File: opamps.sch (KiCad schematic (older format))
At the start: 25 parts, among them U501 TSV324IDT, U502 TSV324IDT, U503 TSV324IDT

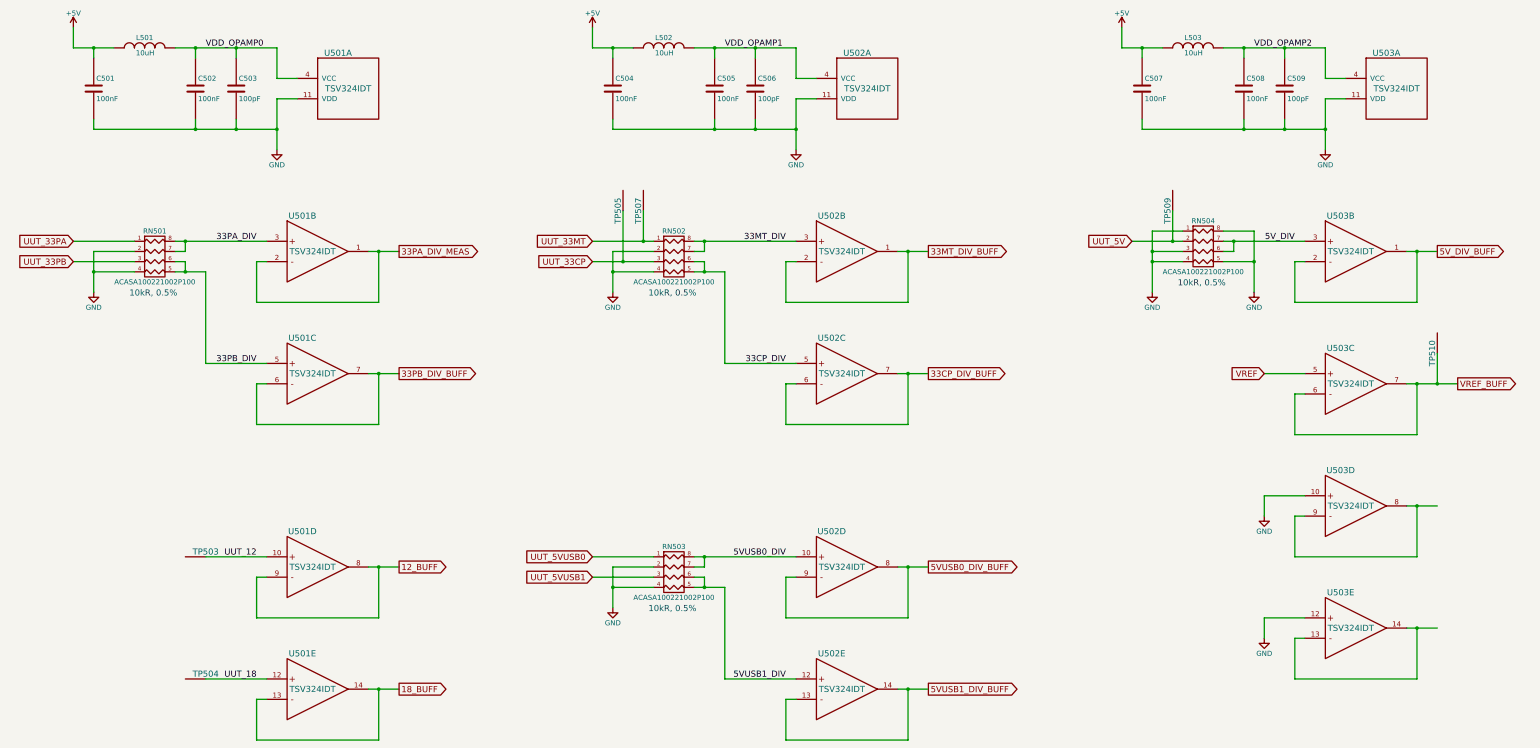
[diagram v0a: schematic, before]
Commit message: significant progress on placement, sch changes for adc routing
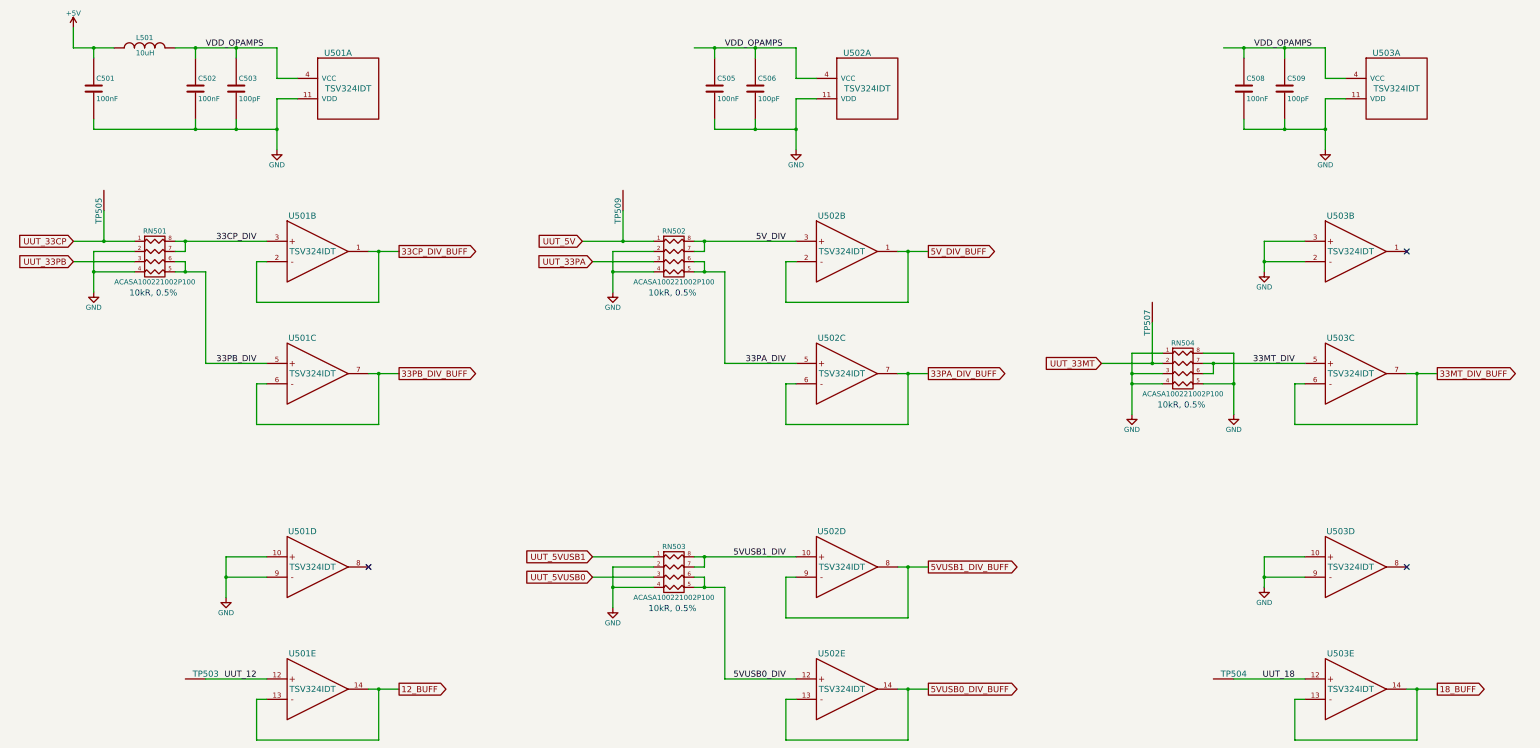
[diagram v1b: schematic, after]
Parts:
- removed C504, C507: 100nF, tm-kicad-lib:SMD-0402-C, symbol TM_C
- removed L502, L503: 10uH, tm-kicad-lib:SMD-0603-R, symbol TM_L
- removed TP510: TP, tm-kicad-lib:Testpoint, symbol TP
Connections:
- net 33PA_DIV_MEAS is gone; now on net 33CP_DIV_BUFF: U501.1, U501.2
- net VDD_OPAMP1 is gone; now on net VDD_OPAMPS: C505.1, C506.1, U502.4 (VCC)
- net VDD_OPAMP2 is gone; now on net VDD_OPAMPS: C508.1, C509.1, U503.4 (VCC)
- net VREF is gone; now on net 33MT_DIV: U503.5
- net VREF_BUFF is gone; now on net 33MT_DIV_BUFF: U503.6, U503.7
- net 12_BUFF: now also U501.13, U501.14; no longer U501.8, U501.9
- net 18_BUFF: now also U503.13, U503.14; no longer U501.13, U501.14
- net 33CP_DIV: now also RN501.7 (R2), RN501.8 (R1), U501.3; no longer RN502.5 (R4), RN502.6 (R3), U502.5
- net 33CP_DIV_BUFF: no longer U502.6, U502.7
- net 33MT_DIV: now also RN504.6 (R3), RN504.7 (R2); no longer RN502.7 (R2), RN502.8 (R1), U502.3
- net 33MT_DIV_BUFF: no longer U502.1, U502.2
- net 33PA_DIV: now also RN502.5 (R4), RN502.6 (R3), U502.5; no longer RN501.7 (R2), RN501.8 (R1), U501.3
- net 5VUSB0_DIV: now also RN503.5 (R4), RN503.6 (R3), U502.12; no longer RN503.7 (R2), RN503.8 (R1), U502.10
- net 5VUSB0_DIV_BUFF: now also U502.13, U502.14; no longer U502.8, U502.9
- net 5VUSB1_DIV: now also RN503.7 (R2), RN503.8 (R1), U502.10; no longer RN503.5 (R4), RN503.6 (R3), U502.12
- net 5VUSB1_DIV_BUFF: now also U502.8, U502.9; no longer U502.13, U502.14
- net 5V_DIV: now also RN502.7 (R2), RN502.8 (R1), U502.3; no longer RN504.6 (R3), RN504.7 (R2), U503.3
- net 5V_DIV_BUFF: now also U502.1, U502.2; no longer U503.1, U503.2
- net GND: now also U501.10, U501.9, U503.2, U503.3, U503.9; no longer U503.12
- net UUT_12: now also U501.12; no longer U501.10
- net UUT_18: now also U503.12; no longer U501.12
- net UUT_33CP: now also RN501.1 (P1); no longer RN502.3 (P3)
- net UUT_33MT: now also RN504.2 (P2); no longer RN502.1 (P1)
- net UUT_33PA: now also RN502.3 (P3); no longer RN501.1 (P1)
- net UUT_5V: now also RN502.1 (P1); no longer RN504.2 (P2)
- net UUT_5VUSB0: now also RN503.3 (P3); no longer RN503.1 (P1)
- net UUT_5VUSB1: now also RN503.1 (P1); no longer RN503.3 (P3)
- net at U503.8: no longer U503.9
- net VDD_OPAMP0 renamed VDD_OPAMPS
- new net 33PA_DIV_BUFF: U502.6, U502.7
- no-connect marks 0 -> 3
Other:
- moved on the sheet: RN504, TP503, TP504, TP505, TP507, TP509, U503C, U503D, U503E

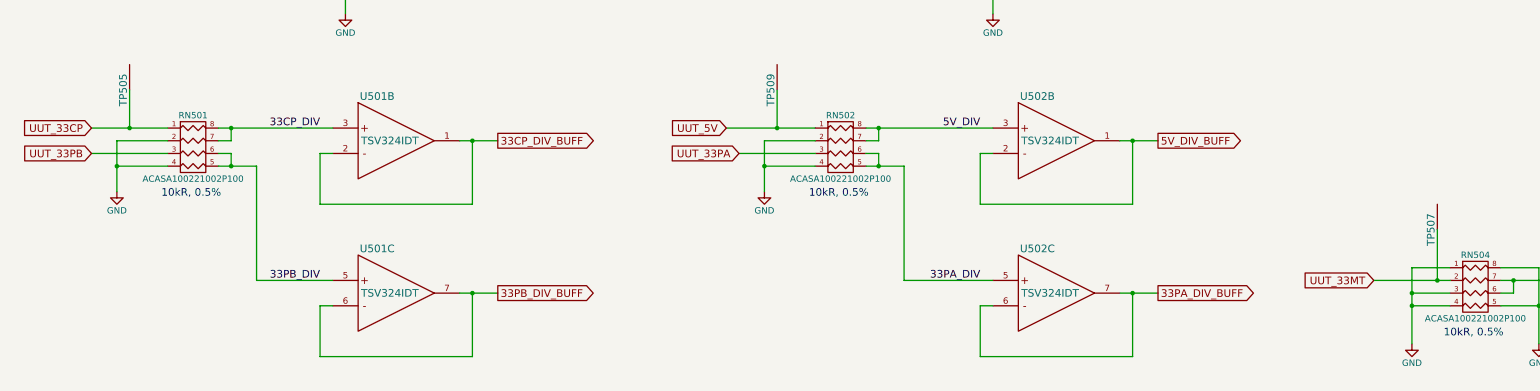
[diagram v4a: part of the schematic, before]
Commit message: mostly routed... time to go back and pin mux
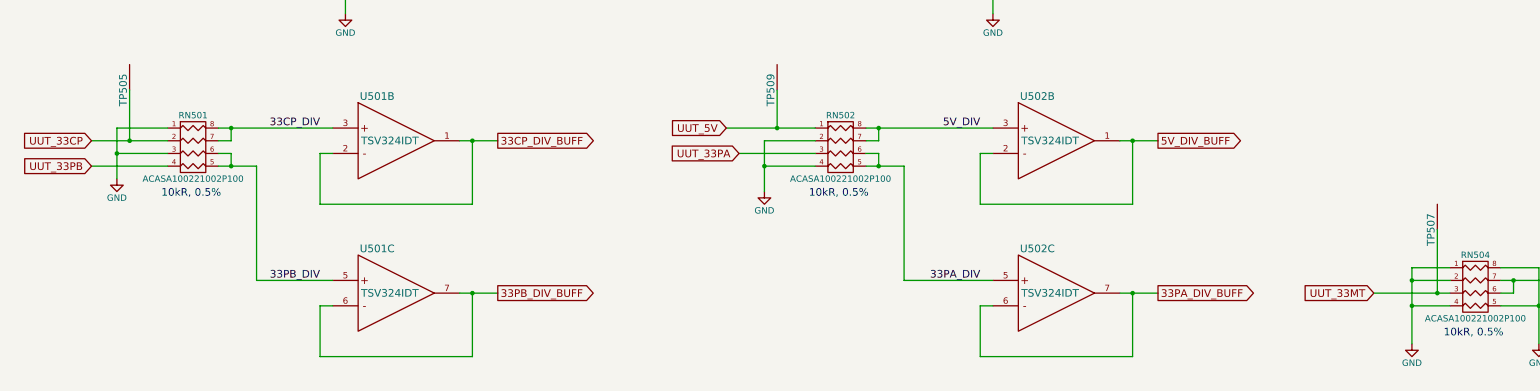
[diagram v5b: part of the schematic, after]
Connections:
- net GND: now also RN501.1 (P1), RN501.3 (P3), RN504.2 (P2); no longer RN501.2 (P2), RN501.4 (P4), RN504.3 (P3)
- net UUT_33CP: now also RN501.2 (P2); no longer RN501.1 (P1)
- net UUT_33MT: now also RN504.3 (P3); no longer RN504.2 (P2)
- net UUT_33PB: now also RN501.4 (P4); no longer RN501.3 (P3)
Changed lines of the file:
@@
 10kR, 0.5%
 $Comp
-L GND #PWR091
+L GND #PWR093
 U 1 1 55403AA7
 P 7000 4200
-F 0 "#PWR091" H 7000 3950 50  0001 C CNN
+F 0 "#PWR093" H 7000 3950 50  0001 C CNN
 F 1 "GND" H 7000 4050 50  0000 C CNN
 F 2 "" H 7000 4200 60  0000 C CNN
@@
 10kR, 0.5%
 $Comp
-L GND #PWR092
+L GND #PWR094
 U 1 1 55403AC9
 P 7000 7300
-F 0 "#PWR092" H 7000 7050 50  0001 C CNN
+F 0 "#PWR094" H 7000 7050 50  0001 C CNN
 F 1 "GND" H 7000 7150 50  0000 C CNN
 F 2 "" H 7000 7300 60  0000 C CNN
@@
 Text GLabel 6800 6800 0    60   Input ~ 0
 UUT_5VUSB1
-Text GLabel 11800 4900 0    60   Input ~ 0
+Text GLabel 11800 5000 0    60   Input ~ 0
 UUT_33MT
-Text GLabel 1700 3700 0    60   Input ~ 0
+Text GLabel 1700 3800 0    60   Input ~ 0
 UUT_33CP
 $Comp
@@
 10kR, 0.5%
 $Comp
-L GND #PWR093
+L GND #PWR095
 U 1 1 554086E2
-P 1900 4200
-F 0 "#PWR093" H 1900 3950 50  0001 C CNN
-F 1 "GND" H 1900 4050 50  0000 C CNN
-F 2 "" H 1900 4200 60  0000 C CNN
-F 3 "" H 1900 4200 60  0000 C CNN
-	1    1900 4200
+P 1900 4100
+F 0 "#PWR095" H 1900 3850 50  0001 C CNN
+F 1 "GND" H 1900 3950 50  0000 C CNN
+F 2 "" H 1900 4100 60  0000 C CNN
+F 3 "" H 1900 4100 60  0000 C CNN
+	1    1900 4100
 	1    0    0    -1
 $EndComp
 Text GLabel 6800 3900 0    60   Input ~ 0
 UUT_33PA
-Text GLabel 1700 3900 0    60   Input ~ 0
+Text GLabel 1700 4000 0    60   Input ~ 0
 UUT_33PB
 Text Label 3500 4900 2    60   ~ 0
@@
 18_BUFF
 $Comp
-L GND #PWR094
+L GND #PWR096
 U 1 1 5540AF3B
 P 8800 2800
-F 0 "#PWR094" H 8800 2550 50  0001 C CNN
+F 0 "#PWR096" H 8800 2550 50  0001 C CNN
 F 1 "GND" H 8800 2650 50  0000 C CNN
 F 2 "" H 8800 2800 60  0000 C CNN
@@
 $EndComp
 $Comp
-L GND #PWR095
+L GND #PWR097
 U 1 1 5540BF80
 P 3700 2800
-F 0 "#PWR095" H 3700 2550 50  0001 C CNN
+F 0 "#PWR097" H 3700 2550 50  0001 C CNN
 F 1 "GND" H 3700 2650 50  0000 C CNN
 F 2 "" H 3700 2800 60  0000 C CNN
@@
 $EndComp
 $Comp
-L +5V #PWR096
+L +5V #PWR098
 U 1 1 5540BFA3
 P 1700 1600
-F 0 "#PWR096" H 1700 1450 50  0001 C CNN
+F 0 "#PWR098" H 1700 1450 50  0001 C CNN
 F 1 "+5V" H 1700 1740 50  0000 C CNN
 F 2 "" H 1700 1600 60  0000 C CNN
@@
 10kR, 0.5%
 $Comp
-L GND #PWR097
+L GND #PWR099
 U 1 1 5540E510
 P 12100 5400
-F 0 "#PWR097" H 12100 5150 50  0001 C CNN
+F 0 "#PWR099" H 12100 5150 50  0001 C CNN
 F 1 "GND" H 12100 5250 50  0000 C CNN
 F 2 "" H 12100 5400 60  0000 C CNN
@@
 UUT_5V
 $Comp
-L GND #PWR098
+L GND #PWR0100
 U 1 1 5540E534
 P 14000 2800
-F 0 "#PWR098" H 14000 2550 50  0001 C CNN
+F 0 "#PWR0100" H 14000 2550 50  0001 C CNN
 F 1 "GND" H 14000 2650 50  0000 C CNN
 F 2 "" H 14000 2800 60  0000 C CNN
@@
 $EndComp
 $Comp
-L GND #PWR099
+L GND #PWR0101
 U 1 1 5540EC4F
 P 13400 7100
-F 0 "#PWR099" H 13400 6850 50  0001 C CNN
+F 0 "#PWR0101" H 13400 6850 50  0001 C CNN
 F 1 "GND" H 13400 6950 50  0000 C CNN
 F 2 "" H 13400 7100 60  0000 C CNN
@@
 $EndComp
 $Comp
-L GND #PWR0100
+L GND #PWR0102
 U 1 1 5540ECBE
 P 3200 7200
-F 0 "#PWR0100" H 3200 6950 50  0001 C CNN
+F 0 "#PWR0102" H 3200 6950 50  0001 C CNN
 F 1 "GND" H 3200 7050 50  0000 C CNN
 F 2 "" H 3200 7200 60  0000 C CNN
@@
 $EndComp
 $Comp
-L GND #PWR0101
+L GND #PWR0103
 U 1 1 55414696
 P 13100 5400
-F 0 "#PWR0101" H 13100 5150 50  0001 C CNN
+F 0 "#PWR0103" H 13100 5150 50  0001 C CNN
 F 1 "GND" H 13100 5250 50  0000 C CNN
 F 2 "" H 13100 5400 60  0000 C CNN
@@
 Connection ~ 7000 4000
 Wire Wire Line
-	11800 4900 12400 4900
-Wire Wire Line
-	1700 3700 2300 3700
-Wire Wire Line
-	2000 3700 2000 3400
+	11800 5000 12400 5000
+Wire Wire Line
+	1700 3800 2300 3800
+Wire Wire Line
+	2000 3800 2000 3400
 Connection ~ 7900 3700
 Wire Wire Line
@@
 	13100 8000 13800 8000
 Wire Wire Line
-	12300 4900 12300 4500
-Connection ~ 12300 4900
-Connection ~ 2000 3700
+	12300 5000 12300 4500
+Connection ~ 12300 5000
+Connection ~ 2000 3800
 Wire Wire Line
 	2700 3700 3600 3700
@@
 	2700 4000 3000 4000
 Wire Wire Line
-	2300 4000 1900 4000
-Wire Wire Line
-	1900 3800 1900 4200
-Wire Wire Line
-	2300 3800 1900 3800
-Connection ~ 1900 4000
+	2300 3900 1900 3900
+Wire Wire Line
+	1900 3700 1900 4100
+Wire Wire Line
+	2300 3700 1900 3700
+Connection ~ 1900 3900
 Connection ~ 2800 3700
 Wire Wire Line
@@
 	12100 4800 12100 5400
 Wire Wire Line
-	12400 5000 12100 5000
+	12400 4900 12100 4900
 Connection ~ 12900 4900
 Wire Wire Line
@@
 Wire Wire Line
 	12400 4800 12100 4800
-Connection ~ 12100 5000
+Connection ~ 12100 4900
 Wire Wire Line
 	12400 5100 12100 5100
@@
 	8000 2600 8800 2600
 $Comp
-L GND #PWR0102
+L GND #PWR0104
 U 1 1 55492A80
 P 13400 4000
-F 0 "#PWR0102" H 13400 3750 50  0001 C CNN
+F 0 "#PWR0104" H 13400 3750 50  0001 C CNN
 F 1 "GND" H 13400 3850 50  0000 C CNN
 F 2 "" H 13400 4000 60  0000 C CNN
@@
 	13400 3700 13400 4000
 Wire Wire Line
-	1700 3900 2300 3900
+	1700 4000 2300 4000
 Wire Wire Line
 	6700 3700 7400 3700
